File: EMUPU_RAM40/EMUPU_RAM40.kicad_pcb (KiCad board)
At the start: 2 copper layers, 99.1 x 85.2 mm, 29 parts, among them J1 Conn_01x20_Socket, J2 Conn_01x20_Socket, J3 Barrel_Jack_Switch, J4 Conn_01x06_Pin, J5 Conn_01x08_Pin, J7 PinHeader_1x06_P2.54mm_Vertic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, SW1 SW_SPDT, SW2 SW_SPST, U1 PIC18F47Q43-IP, U2 628128

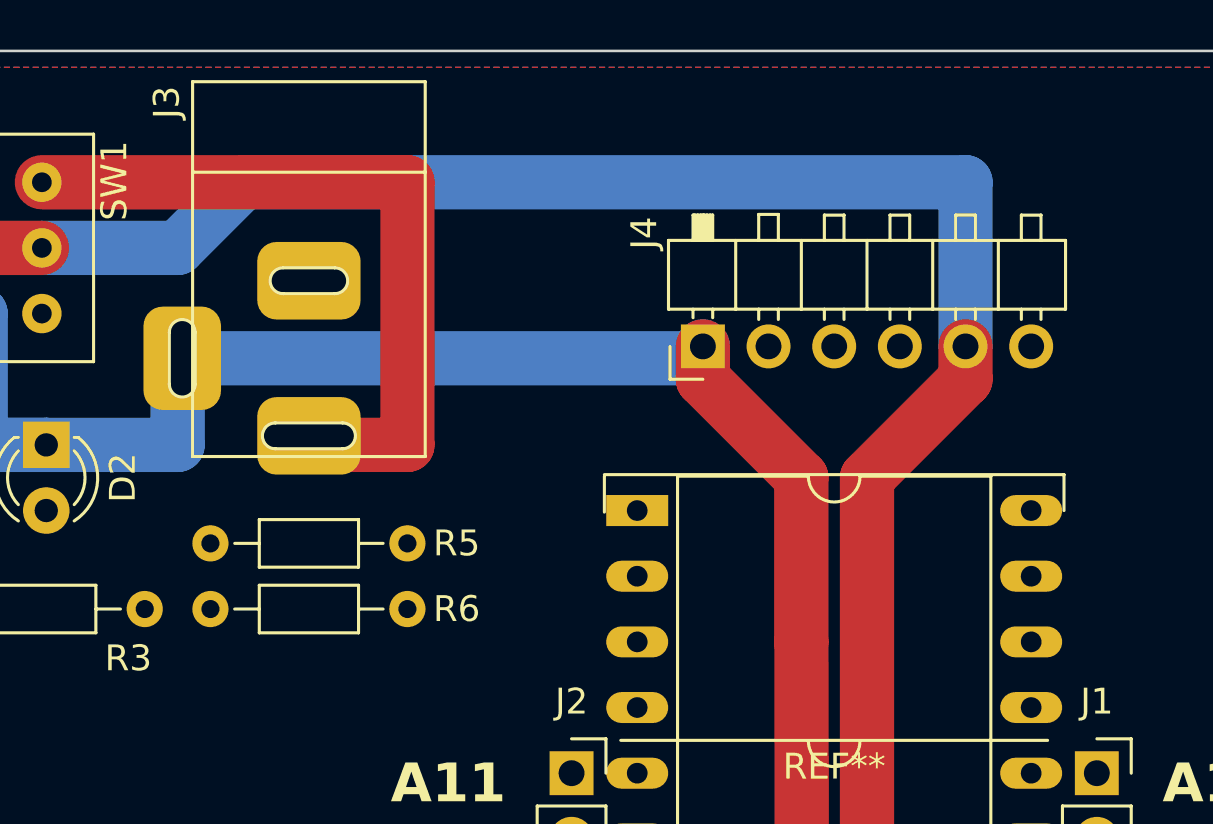
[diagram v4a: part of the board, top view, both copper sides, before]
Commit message: Correct Serial 6pin connections
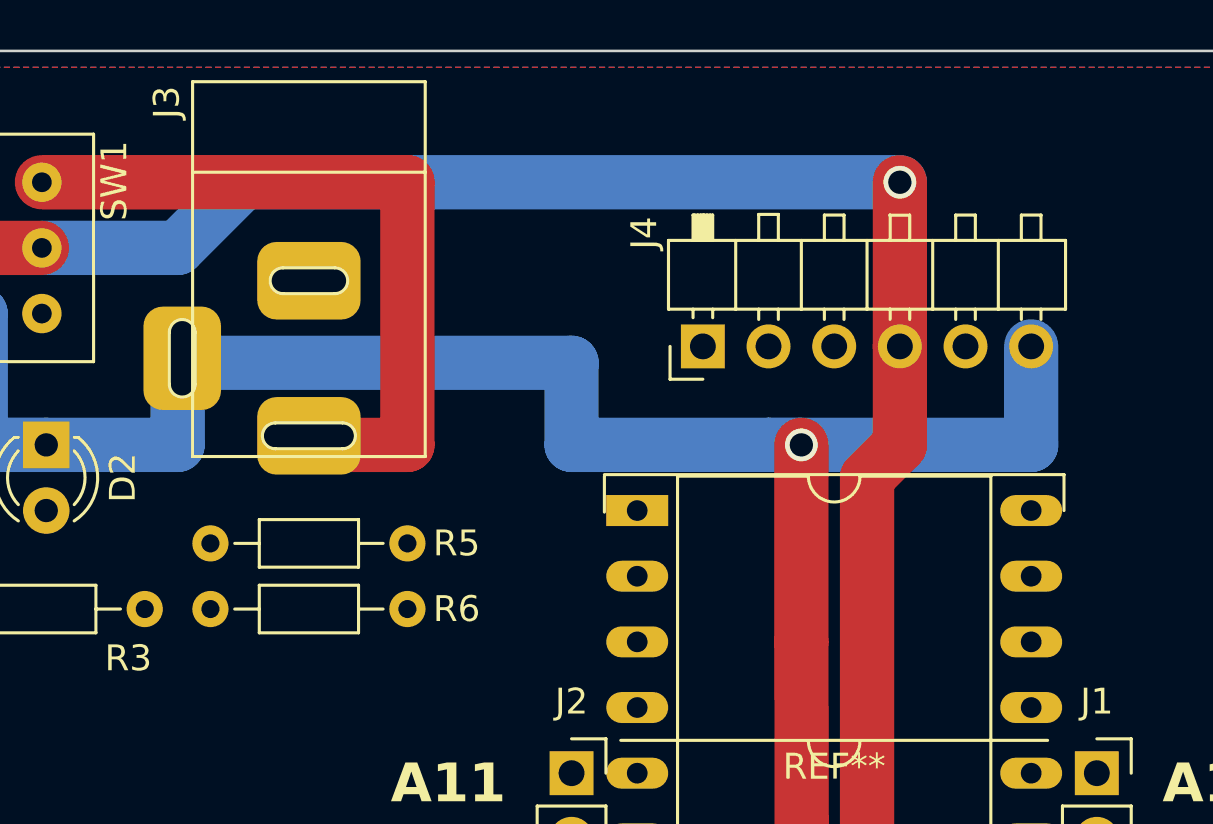
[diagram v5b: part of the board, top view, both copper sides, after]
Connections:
- J4 pad 1: GND -> unconnected-(J4-Pin_1-Pad1)
- J4 pad 4: unconnected-(J4-Pin_4-Pad4) -> VCC
- J4 pad 5: VCC -> unconnected-(J4-Pin_5-Pad5)
- J4 pad 6: unconnected-(J4-Pin_6-Pad6) -> GND
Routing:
- net GND: track 323.9 -> 339.3 mm, vias 5 -> 6
- net VCC: track 326.5 -> 322.9 mm, vias 5 -> 6
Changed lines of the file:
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@@
   (net 51 "unconnected-(J5-Pin_7-Pad7)")
   (net 52 "unconnected-(J5-Pin_8-Pad8)")
-  (net 53 "unconnected-(J4-Pin_4-Pad4)")
-  (net 54 "unconnected-(J4-Pin_6-Pad6)")
+  (net 53 "unconnected-(J4-Pin_1-Pad1)")
+  (net 54 "unconnected-(J4-Pin_5-Pad5)")
   (net 55 "unconnected-(J3-Pad3)")
   (net 56 "/~{INT}")
@@
       (stroke (width 0.1) (type solid)) (layer "F.Fab"))
     (pad "1" thru_hole rect (at 0 0 90) (size 1.7 1.7) (drill 1) (layers "*.Cu" "*.Mask")
-      (net 6 "GND") (pinfunction "Pin_1") (pintype "passive"))
+      (net 53 "unconnected-(J4-Pin_1-Pad1)") (pinfunction "Pin_1") (pintype "passive+no_connect"))
     (pad "2" thru_hole oval (at 0 2.54 90) (size 1.7 1.7) (drill 1) (layers "*.Cu" "*.Mask")
       (net 17 "Net-(J4-Pin_2)") (pinfunction "Pin_2") (pintype "passive"))
@@
       (net 43 "Net-(D1-K)") (pinfunction "Pin_3") (pintype "passive"))
     (pad "4" thru_hole oval (at 0 7.62 90) (size 1.7 1.7) (drill 1) (layers "*.Cu" "*.Mask")
-      (net 53 "unconnected-(J4-Pin_4-Pad4)") (pinfunction "Pin_4") (pintype "passive+no_connect"))
+      (net 1 "VCC") (pinfunction "Pin_4") (pintype "passive"))
     (pad "5" thru_hole oval (at 0 10.16 90) (size 1.7 1.7) (drill 1) (layers "*.Cu" "*.Mask")
-      (net 1 "VCC") (pinfunction "Pin_5") (pintype "passive"))
+      (net 54 "unconnected-(J4-Pin_5-Pad5)") (pinfunction "Pin_5") (pintype "passive+no_connect"))
     (pad "6" thru_hole oval (at 0 12.7 90) (size 1.7 1.7) (drill 1) (layers "*.Cu" "*.Mask")
-      (net 54 "unconnected-(J4-Pin_6-Pad6)") (pinfunction "Pin_6") (pintype "passive+no_connect"))
+      (net 6 "GND") (pinfunction "Pin_6") (pintype "passive"))
     (model "${KICAD6_3DMODEL_DIR}/Connector_PinHeader_2.54mm.3dshapes/PinHeader_1x06_P2.54mm_Horizontal.wrl"
       (offset (xyz 0 0 0))
@@
     (effects (font (size 1.5 1.5) (thickness 0.3) bold) (justify right bottom))
   )
-  (segment (start 171.45 78.74) (end 171.45 77.47) (width 2.1) (layer "F.Cu") (net 1))
   (segment (start 143.34 104.14) (end 136.99 104.14) (width 2.1) (layer "F.Cu") (net 1))
   (segment (start 136.99 104.14) (end 137.16 146.05) (width 2.1) (layer "F.Cu") (net 1))
+  (segment (start 168.91 71.12) (end 168.91 77.47) (width 2.1) (layer "F.Cu") (net 1))
   (segment (start 149.86 119.38) (end 149.86 145.415) (width 2.1) (layer "F.Cu") (net 1))
   (segment (start 118.11 73.66) (end 135.72 73.66) (width 2.1) (layer "F.Cu") (net 1))
   (segment (start 156.21 119.38) (end 149.86 119.38) (width 2.1) (layer "F.Cu") (net 1))
-  (segment (start 167.64 82.55) (end 171.45 78.74) (width 2.1) (layer "F.Cu") (net 1))
+  (segment (start 168.91 77.47) (end 168.91 81.28) (width 2.1) (layer "F.Cu") (net 1))
   (segment (start 167.64 145.415) (end 167.64 82.55) (width 2.1) (layer "F.Cu") (net 1))
+  (segment (start 168.91 81.28) (end 167.64 82.55) (width 2.1) (layer "F.Cu") (net 1))
   (segment (start 109.22 119.38) (end 109.22 144.78) (width 2.1) (layer "F.Cu") (net 1))
   (segment (start 109.22 114.3) (end 109.22 119.38) (width 2.1) (layer "F.Cu") (net 1))
@@
   (via (at 109.22 144.78) (size 1.27) (drill 0.9) (layers "F.Cu" "B.Cu") (net 1))
   (via (at 149.86 145.415) (size 1.27) (drill 0.9) (layers "F.Cu" "B.Cu") (net 1))
+  (via (at 168.91 71.12) (size 1.27) (drill 0.9) (layers "F.Cu" "B.Cu") (net 1))
+  (segment (start 140.97 73.66) (end 143.51 71.12) (width 2.1) (layer "B.Cu") (net 1))
   (segment (start 137.16 145.415) (end 149.86 145.415) (width 2.1) (layer "B.Cu") (net 1))
   (segment (start 100.16 119.38) (end 97.79 119.4) (width 2.1) (layer "B.Cu") (net 1))
   (segment (start 95.25 119.38) (end 97.77 119.38) (width 0.1524) (layer "B.Cu") (net 1))
   (segment (start 97.77 119.38) (end 97.79 119.4) (width 0.1524) (layer "B.Cu") (net 1))
-  (segment (start 140.97 73.66) (end 143.51 71.12) (width 2.1) (layer "B.Cu") (net 1))
-  (segment (start 143.51 71.12) (end 171.45 71.12) (width 2.1) (layer "B.Cu") (net 1))
-  (segment (start 135.72 73.66) (end 140.97 73.66) (width 2.1) (layer "B.Cu") (net 1))
+  (segment (start 143.51 71.12) (end 168.91 71.12) (width 2.1) (layer "B.Cu") (net 1))
   (segment (start 100.16 119.38) (end 109.22 119.38) (width 2.1) (layer "B.Cu") (net 1))
   (segment (start 109.22 145.415) (end 137.16 145.415) (width 2.1) (layer "B.Cu") (net 1))
+  (segment (start 135.72 73.66) (end 140.97 73.66) (width 2.1) (layer "B.Cu") (net 1))
   (segment (start 118.11 114.34) (end 109.22 114.3) (width 2.1) (layer "B.Cu") (net 1))
   (segment (start 149.86 145.415) (end 167.64 145.415) (width 2.1) (layer "B.Cu") (net 1))
-  (segment (start 171.45 71.12) (end 171.45 77.47) (width 2.1) (layer "B.Cu") (net 1))
+  (segment (start 165.1 88.9) (end 165.14 106.68) (width 2.1) (layer "F.Cu") (net 6))
+  (segment (start 165.1 81.28) (end 165.1 88.9) (width 2.1) (layer "F.Cu") (net 6))
   (segment (start 106.68 121.92) (end 106.68 148.59) (width 2.1) (layer "F.Cu") (net 6))
-  (segment (start 161.29 77.47) (end 161.29 78.74) (width 2.1) (layer "F.Cu") (net 6))
   (segment (start 165.14 147.28) (end 165.14 106.68) (width 2.1) (layer "F.Cu") (net 6))
   (segment (start 165.1 147.955) (end 165.14 147.28) (width 2.1) (layer "F.Cu") (net 6))
   (segment (start 134.48 142.24) (end 128.1 142.24) (width 2.1) (layer "F.Cu") (net 6))
-  (segment (start 161.29 78.74) (end 165.1 82.55) (width 2.1) (layer "F.Cu") (net 6))
-  (segment (start 165.1 82.55) (end 165.1 88.9) (width 2.1) (layer "F.Cu") (net 6))
-  (segment (start 165.1 88.9) (end 165.14 106.68) (width 2.1) (layer "F.Cu") (net 6))
   (segment (start 134.48 147.955) (end 134.48 142.24) (width 2.1) (layer "F.Cu") (net 6))
   (segment (start 106.68 116.84) (end 106.68 121.92) (width 2.1) (layer "F.Cu") (net 6))
   (via (at 134.48 147.955) (size 1.27) (drill 0.9) (layers "F.Cu" "B.Cu") (net 6))
   (via (at 165.1 147.955) (size 1.27) (drill 0.9) (layers "F.Cu" "B.Cu") (net 6))
+  (via (at 165.1 81.28) (size 1.27) (drill 0.9) (layers "F.Cu" "B.Cu") (net 6))
   (via (at 106.68 121.92) (size 1.27) (drill 0.9) (layers "F.Cu" "B.Cu") (net 6))
   (via (at 106.68 148.59) (size 1.27) (drill 0.9) (layers "F.Cu" "B.Cu") (net 6))
@@
   (segment (start 118.11 116.84) (end 106.68 116.84) (width 2.1) (layer "B.Cu") (net 6))
   (segment (start 163.195 147.955) (end 134.48 147.955) (width 2.1) (layer "B.Cu") (net 6))
-  (segment (start 160.83 77.93) (end 161.29 77.47) (width 2.1) (layer "B.Cu") (net 6))
   (segment (start 106.66 121.9) (end 106.68 121.92) (width 2.1) (layer "B.Cu") (net 6))
   (segment (start 97.79 121.9) (end 106.66 121.9) (width 2.1) (layer "B.Cu") (net 6))
@@
   (segment (start 133.35 81.28) (end 135.89 81.28) (width 2.1) (layer "B.Cu") (net 6))
   (segment (start 182.88 121.92) (end 176.53 121.92) (width 2.1) (layer "B.Cu") (net 6))
+  (segment (start 163.83 81.28) (end 165.1 81.28) (width 2.1) (layer "B.Cu") (net 6))
+  (segment (start 141.325 78.105) (end 156.21 78.105) (width 2.1) (layer "B.Cu") (net 6))
   (segment (start 165.1 147.955) (end 163.195 147.955) (width 2.1) (layer "B.Cu") (net 6))
-  (segment (start 141.15 77.93) (end 160.83 77.93) (width 2.1) (layer "B.Cu") (net 6))
+  (segment (start 156.21 78.105) (end 156.21 81.28) (width 2.1) (layer "B.Cu") (net 6))
+  (segment (start 163.83 81.28) (end 173.99 81.28) (width 2.1) (layer "B.Cu") (net 6))
+  (segment (start 141.15 77.93) (end 141.325 78.105) (width 2.1) (layer "B.Cu") (net 6))
   (segment (start 128.27 76.2) (end 124.46 76.2) (width 2.1) (layer "B.Cu") (net 6))
+  (segment (start 156.21 81.28) (end 163.83 81.28) (width 2.1) (layer "B.Cu") (net 6))
   (segment (start 106.68 147.955) (end 134.48 147.955) (width 2.1) (layer "B.Cu") (net 6))
   (segment (start 133.35 76.2) (end 133.35 81.28) (width 2.1) (layer "B.Cu") (net 6))
   (segment (start 140.97 78.11) (end 141.15 77.93) (width 2.1) (layer "B.Cu") (net 6))
   (segment (start 121.77 81.28) (end 135.89 81.28) (width 2.1) (layer "B.Cu") (net 6))
+  (segment (start 173.99 81.28) (end 173.99 77.47) (width 2.1) (layer "B.Cu") (net 6))
   (segment (start 124.46 73.66) (end 115.57 73.66) (width 2.1) (layer "B.Cu") (net 6))
   (segment (start 140.97 81.28) (end 140.97 78.11) (width 2.1) (layer "B.Cu") (net 6))
